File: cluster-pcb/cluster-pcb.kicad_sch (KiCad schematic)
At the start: 0 parts

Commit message: Add address
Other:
- added sheet address (address.kicad_sch)
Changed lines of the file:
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@@
     (title "cluster-pcb")
     (date "2024-08-26")
-    (rev "1.1")
+    (rev "1.2")
     (company "Howard Hughes Medical Institute")
   )
@@
       )
     )
+  )
+  (sheet (at 74.93 140.97) (size 21.59 10.16) (fields_autoplaced)
+    (stroke (width 0.1524) (type solid))
+    (fill (color 0 0 0 0.0000))
+    (property "Sheetname" "address" (at 74.93 140.2584 0)
+      (effects (font (size 1.27 1.27)) (justify left bottom))
+    )
+    (property "Sheetfile" "address.kicad_sch" (at 74.93 151.7146 0)
+      (effects (font (size 1.27 1.27)) (justify left top))
+    )
+    (instances
+      (project "cluster-pcb"
+        (path "/df2b2e89-e055-4140-95de-f1df723db034" (page "12"))
+      )
+    )

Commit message: Add i2c pullups
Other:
- sheet address ports: added +3.3V, GND, SCL, SDA; removed none
- sheet microcontroller ports: added SCL, SDA; removed none
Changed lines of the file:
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@@
+    (stroke (width 0) (type default))
+  )
+  (wire (pts (xy 72.39 153.67) (xy 74.93 153.67))
     (stroke (width 0) (type default))
   )
@@
     (stroke (width 0) (type default))
   )
+  (wire (pts (xy 72.39 146.05) (xy 74.93 146.05))
+    (stroke (width 0) (type default))
+  )
   (wire (pts (xy 135.89 62.23) (xy 138.43 62.23))
     (stroke (width 0) (type default))
@@
     (stroke (width 0) (type default))
   )
+  (wire (pts (xy 72.39 151.13) (xy 74.93 151.13))
+    (stroke (width 0) (type default))
+  )
   (wire (pts (xy 181.61 59.69) (xy 184.15 59.69))
     (stroke (width 0) (type default))
@@
     (stroke (width 0) (type default))
   )
+  (wire (pts (xy 72.39 74.93) (xy 74.93 74.93))
+    (stroke (width 0) (type default))
+  )
   (wire (pts (xy 99.06 64.77) (xy 96.52 64.77))
     (stroke (width 0) (type default))
@@
     (stroke (width 0) (type default))
   )
+  (wire (pts (xy 72.39 72.39) (xy 74.93 72.39))
+    (stroke (width 0) (type default))
+  )
   (wire (pts (xy 135.89 35.56) (xy 138.43 35.56))
     (stroke (width 0) (type default))
@@
     (stroke (width 0) (type default))
   )
+  (wire (pts (xy 72.39 143.51) (xy 74.93 143.51))
+    (stroke (width 0) (type default))
+  )
   (wire (pts (xy 135.89 128.27) (xy 138.43 128.27))
     (stroke (width 0) (type default))
@@
     (effects (font (size 1.27 1.27)) (justify right bottom))
   )
+  (label "SCL" (at 72.39 151.13 180) (fields_autoplaced)
+    (effects (font (size 1.27 1.27)) (justify right bottom))
+  )
   (label "ENABLE_TX_1" (at 135.89 74.93 180) (fields_autoplaced)
     (effects (font (size 1.27 1.27)) (justify right bottom))
@@
     (effects (font (size 1.27 1.27)) (justify right bottom))
   )
+  (label "GND" (at 72.39 146.05 180) (fields_autoplaced)
+    (effects (font (size 1.27 1.27)) (justify right bottom))
+  )
   (label "~{ENABLE_RX_4}" (at 99.06 113.03 0) (fields_autoplaced)
     (effects (font (size 1.27 1.27)) (justify left bottom))
@@
     (effects (font (size 1.27 1.27)) (justify right bottom))
   )
+  (label "SCL" (at 72.39 72.39 180) (fields_autoplaced)
+    (effects (font (size 1.27 1.27)) (justify right bottom))
+  )
   (label "+5V" (at 181.61 33.02 180) (fields_autoplaced)
     (effects (font (size 1.27 1.27)) (justify right bottom))
@@
     (effects (font (size 1.27 1.27)) (justify left bottom))
   )
+  (label "+3.3V" (at 72.39 143.51 180) (fields_autoplaced)
+    (effects (font (size 1.27 1.27)) (justify right bottom))
+  )
+  (label "SDA" (at 72.39 74.93 180) (fields_autoplaced)
+    (effects (font (size 1.27 1.27)) (justify right bottom))
+  )
   (label "~{ENABLE_RX_6}" (at 181.61 106.68 180) (fields_autoplaced)
+    (effects (font (size 1.27 1.27)) (justify right bottom))
+  )
+  (label "SDA" (at 72.39 153.67 180) (fields_autoplaced)
     (effects (font (size 1.27 1.27)) (justify right bottom))
   )
@@
     )
   )
-  (sheet (at 74.93 140.97) (size 21.59 10.16) (fields_autoplaced)
+  (sheet (at 74.93 140.97) (size 21.59 15.24) (fields_autoplaced)
     (stroke (width 0.1524) (type solid))
     (fill (color 0 0 0 0.0000))
@@
       (effects (font (size 1.27 1.27)) (justify left bottom))
     )
-    (property "Sheetfile" "address.kicad_sch" (at 74.93 151.7146 0)
+    (property "Sheetfile" "address.kicad_sch" (at 74.93 156.7946 0)
       (effects (font (size 1.27 1.27)) (justify left top))
+    )
+    (pin "SDA" bidirectional (at 74.93 153.67 180)
+      (effects (font (size 1.27 1.27)) (justify left))
+    )
+    (pin "SCL" input (at 74.93 151.13 180)
+      (effects (font (size 1.27 1.27)) (justify left))
+    )
+    (pin "GND" passive (at 74.93 146.05 180)
+      (effects (font (size 1.27 1.27)) (justify left))
+    )
+    (pin "+3.3V" passive (at 74.93 143.51 180)
+      (effects (font (size 1.27 1.27)) (justify left))
     )
     (instances
@@
       (effects (font (size 1.27 1.27)) (justify right))
     )
+    (pin "SCL" output (at 74.93 72.39 180)
+      (effects (font (size 1.27 1.27)) (justify left))
+    )
+    (pin "SDA" bidirectional (at 74.93 74.93 180)
+      (effects (font (size 1.27 1.27)) (justify left))
+    )
     (instances

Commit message: Update schematic
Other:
- added sheet audio (audio.kicad_sch)
- added sheet multiplexer (multiplexer.kicad_sch)
- sheet microcontroller ports: added AUDIO, ENABLE_POWER, ENABLE_TXRX_0, ENABLE_TXRX_1, ENABLE_TXRX_2, ENABLE_TXRX_3, ENABLE_TXRX_4, ENABLE_TXRX_5, ENABLE_TXRX_6, MUX_ADDRESS_0, MUX_ADDRESS_1, MUX_ADDRESS_2; removed ENABLE_TX_0, ENABLE_TX_1, ENABLE_TX_2, ENABLE_TX_3, ENABLE_TX_4, ENABLE_TX_5, ENABLE_TX_6, ENABLE_VCC, ~{ENABLE_RX_0}, ~{ENABLE_RX_1}, ~{ENABLE_RX_2}, ~{ENABLE_RX_3}, ~{ENABLE_RX_4}, ~{ENABLE_RX_5}, ~{ENABLE_RX_6}
- sheet power ports: added VBB; removed ENABLE_VCC, VCC
- sheet prism-0 ports: added ENABLE_POWER, ENABLE_TXRX; removed ENABLE_TX, ~{ENABLE_RX}
- sheet prism-1 ports: added ENABLE_POWER, ENABLE_TXRX; removed ENABLE_TX, ~{ENABLE_RX}
- sheet prism-2 ports: added ENABLE_POWER, ENABLE_TXRX; removed ENABLE_TX, ~{ENABLE_RX}
- sheet prism-3 ports: added ENABLE_POWER, ENABLE_TXRX; removed ENABLE_TX, ~{ENABLE_RX}
- sheet prism-4 ports: added ENABLE_POWER, ENABLE_TXRX; removed ENABLE_TX, ~{ENABLE_RX}
- sheet prism-5 ports: added ENABLE_POWER, ENABLE_TXRX; removed ENABLE_TX, ~{ENABLE_RX}
- sheet prism-6 ports: added ENABLE_POWER, ENABLE_TXRX; removed ENABLE_TX, ~{ENABLE_RX}

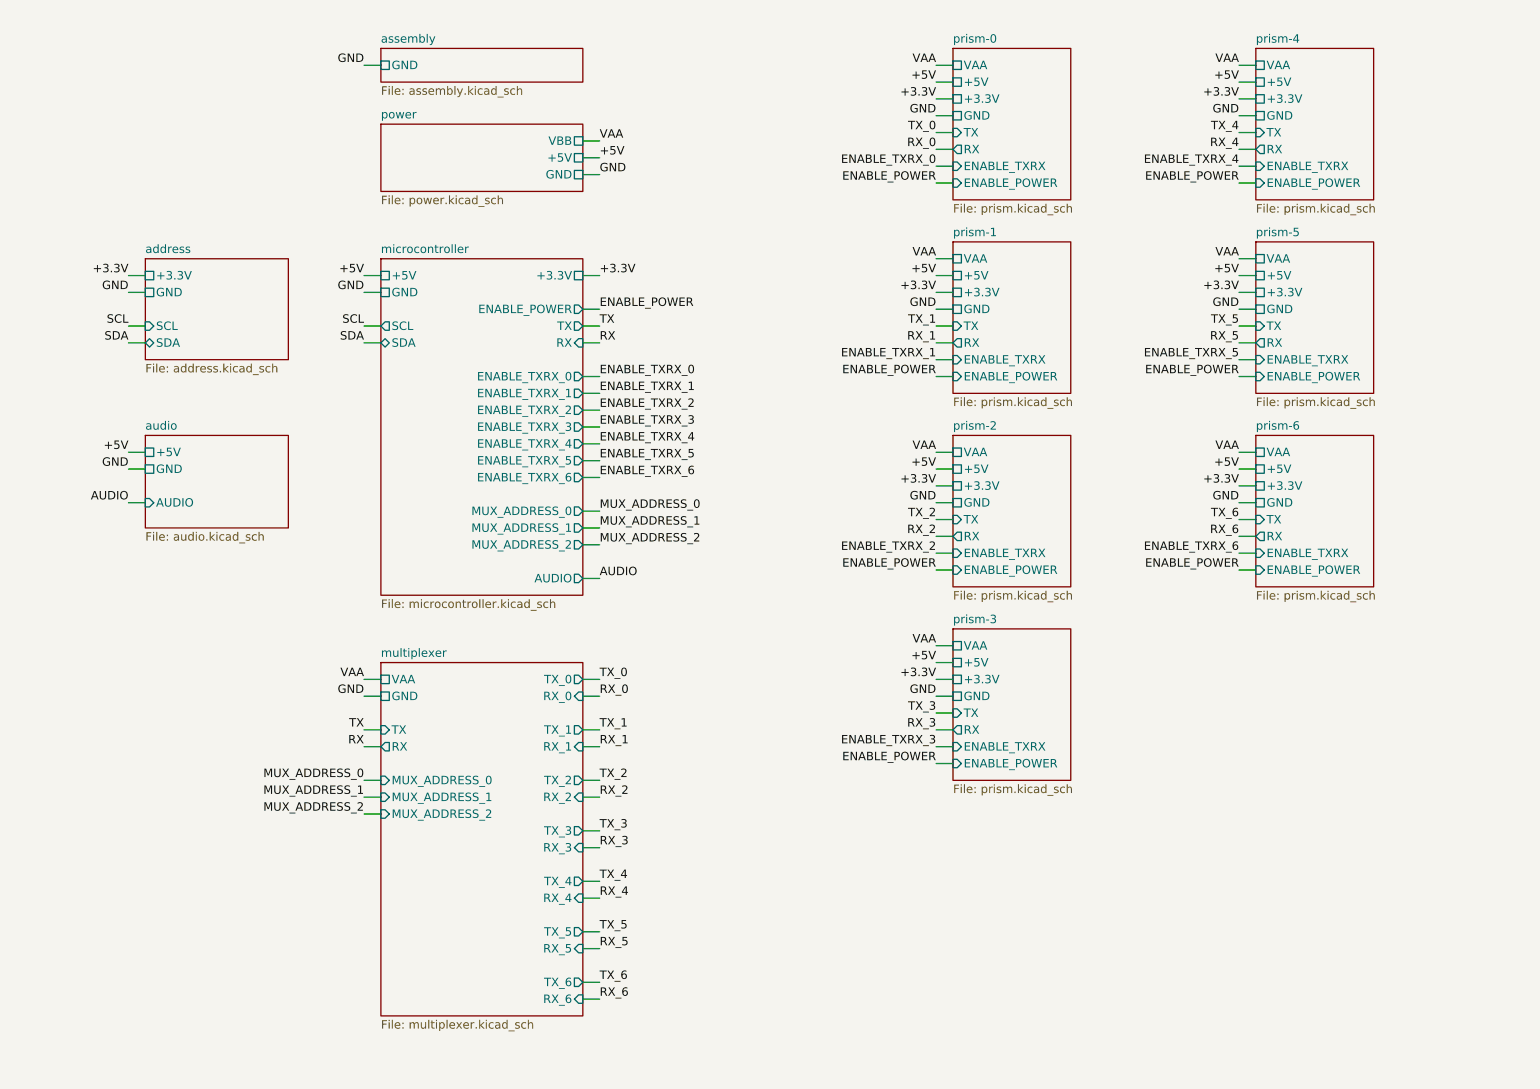
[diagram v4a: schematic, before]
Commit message: Fix ERC issues
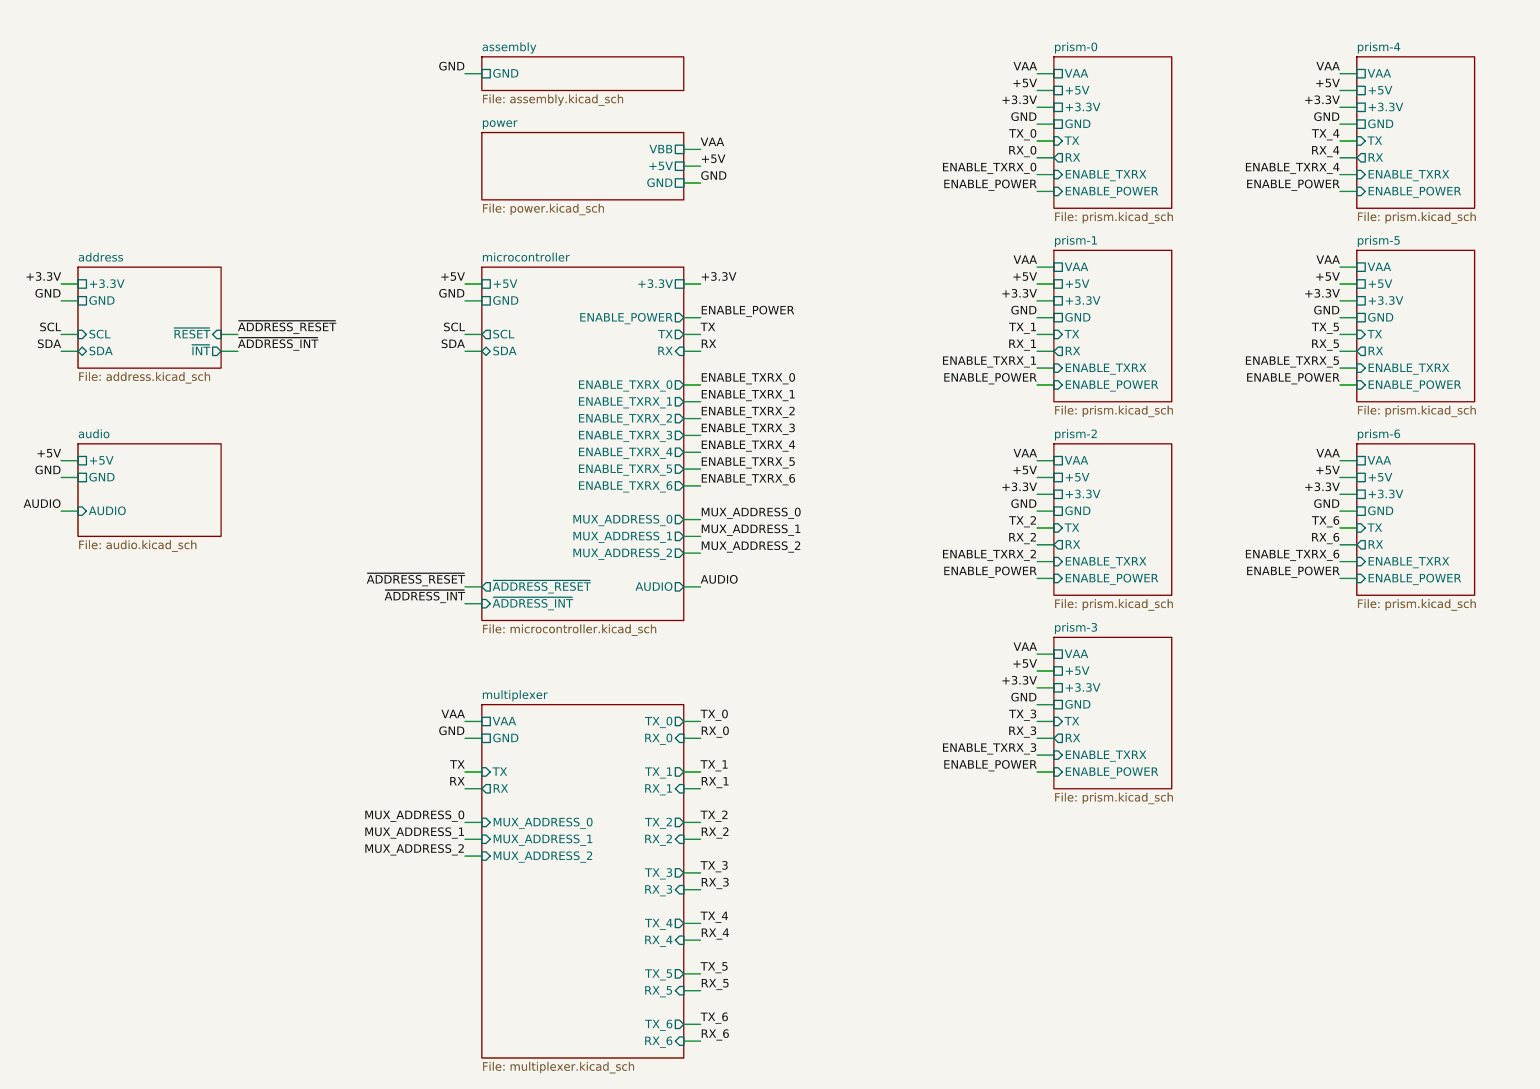
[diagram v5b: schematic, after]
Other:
- sheet address ports: added ~{INT}, ~{RESET}; removed none
- sheet microcontroller ports: added ~{ADDRESS_INT}, ~{ADDRESS_RESET}; removed none
